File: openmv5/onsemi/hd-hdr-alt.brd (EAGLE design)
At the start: 35.6 x 16.5 mm, 54 parts, among them IC1 AR0132AT6C00XPEA0, IC2 TLV62568PDDCR, IC3 MIC5365-2.8YC5-TR, J1 DF12-36-DP, Q1 PMXB120EPEZ

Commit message: Finish out new onsemi cameras
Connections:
- removed net DCMI_D12: J1.8
- removed net DCMI_D13: J1.6
- net GND: now also J1.6, J1.8
- net SPI_MISO: now also IC1.P$35
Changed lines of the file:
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@@
 <contactref element="IC1" pad="P$55"/>
 <contactref element="IC1" pad="P$7"/>
+<contactref element="J1" pad="6"/>
+<contactref element="J1" pad="8"/>
 <wire x1="21.28" y1="11.755" x2="23.495" y2="12.9015" width="0" layer="19" extent="1-1"/>
 <wire x1="21.03" y1="10.8999" x2="21.28" y2="11.755" width="0" layer="19" extent="1-16"/>
@@
 <wire x1="20.197" y1="9.525" x2="20.28" y2="9.755" width="0" layer="19" extent="1-16"/>
 <wire x1="20.824" y1="13.208" x2="21.28" y2="11.755" width="0" layer="19" extent="1-1"/>
+<wire x1="21.03" y1="14.5001" x2="20.824" y2="13.208" width="0" layer="19" extent="1-16"/>
+<wire x1="20.53" y1="14.5001" x2="21.03" y2="14.5001" width="0" layer="19" extent="16-16"/>
+<wire x1="19.2485" y1="14.0335" x2="20.53" y2="14.5001" width="0" layer="19" extent="1-16"/>
+<wire x1="18.8" y1="13.208" x2="19.2485" y2="14.0335" width="0" layer="19" extent="1-1"/>
+<wire x1="18.288" y1="13.712" x2="18.8" y2="13.208" width="0" layer="19" extent="1-1"/>
 <wire x1="21.336" y1="8.005" x2="21.34" y2="9.525" width="0" layer="19" extent="16-16"/>
 <wire x1="20.193" y1="8.005" x2="21.336" y2="8.005" width="0" layer="19" extent="16-16"/>
@@
 <wire x1="20.7755" y1="2.54" x2="20.32" y2="4.195" width="0" layer="19" extent="1-16"/>
 <wire x1="23.0505" y1="7.6915" x2="21.336" y2="8.005" width="0" layer="19" extent="1-16"/>
-<wire x1="19.2485" y1="14.0335" x2="20.824" y2="13.208" width="0" layer="19" extent="1-1"/>
-<wire x1="18.8" y1="13.208" x2="19.2485" y2="14.0335" width="0" layer="19" extent="1-1"/>
-<wire x1="18.288" y1="13.712" x2="18.8" y2="13.208" width="0" layer="19" extent="1-1"/>
 <wire x1="15.53" y1="10.8999" x2="17.53" y2="10.8999" width="0" layer="19" extent="16-16"/>
 <wire x1="22.626" y1="1.778" x2="20.7755" y2="2.54" width="0" layer="19" extent="1-16"/>
@@
 <signal name="SPI_MISO" class="4">
 <contactref element="J1" pad="15"/>
+<contactref element="IC1" pad="P$35"/>
+<wire x1="17.28" y1="7.755" x2="18.53" y2="10.8999" width="0" layer="19" extent="1-16"/>
 </signal>
 <signal name="SPI_MOSI" class="4">
@@
 <wire x1="16.28" y1="6.755" x2="16.53" y2="14.5001" width="0" layer="19" extent="1-16"/>
 </signal>
-<signal name="DCMI_D13" class="4">
-<contactref element="J1" pad="6"/>
-</signal>
-<signal name="DCMI_D12" class="4">
-<contactref element="J1" pad="8"/>
-</signal>
 <signal name="SW" class="3">

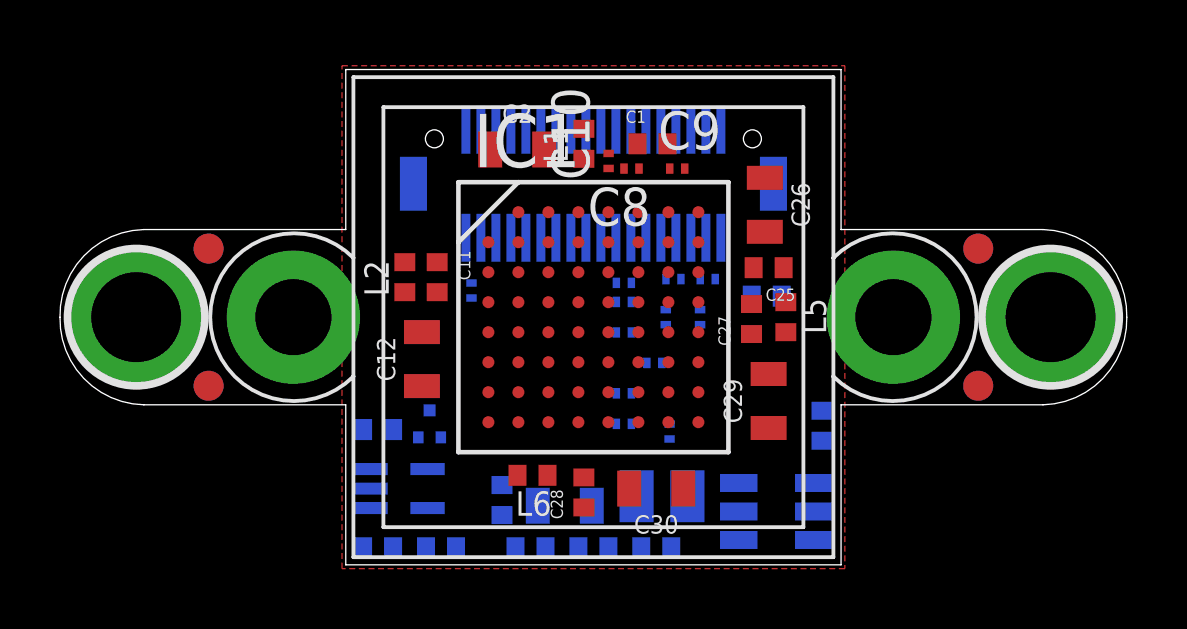
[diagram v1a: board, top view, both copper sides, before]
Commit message: Update camera modules to use different non-flippable pmosfet
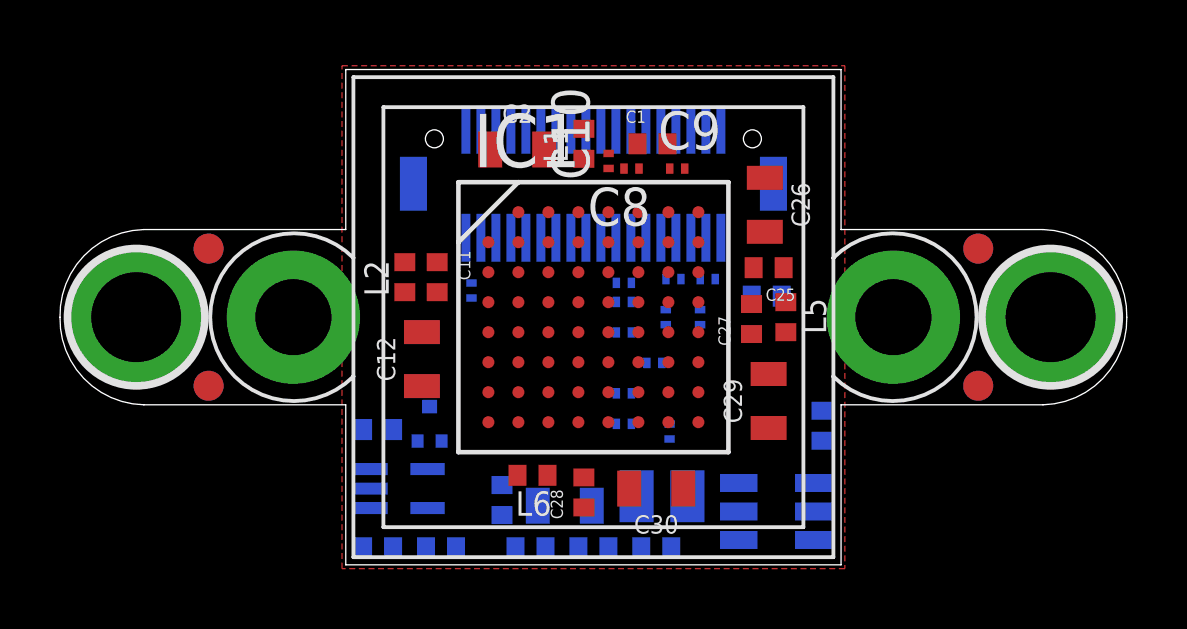
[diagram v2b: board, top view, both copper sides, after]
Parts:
- Q1: value PMXB120EPEZ -> SSM3J15FV,L3F; device PMXB120EPEZ:PMXB120EPEZ -> SSM3J15FV_L3F:SSM3J15FVL3F
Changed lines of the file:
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@@
 <attribute name="VALUE" x="15.24" y="12.954" size="0.6096" layer="27" font="vector" ratio="20" align="top-center"/>
 </element>
-<element name="Q1" library="PMXB120EPEZ" package="PMXB120EPEZ" value="PMXB120EPEZ" x="12.319" y="4.699" smashed="yes" rot="MR0">
-<attribute name="DESCRIPTION" value="MOSFET 30 V, P-channel Trench MOSFET" x="15.367" y="4.699" size="1.778" layer="28" rot="MR0" display="off"/>
-<attribute name="HEIGHT" value="0.4mm" x="15.367" y="4.699" size="1.778" layer="28" rot="MR0" display="off"/>
-<attribute name="MANUFACTURER_NAME" value="Nexperia" x="15.367" y="4.699" size="1.778" layer="28" rot="MR0" display="off"/>
-<attribute name="MANUFACTURER_PART_NUMBER" value="PMXB120EPEZ" x="15.367" y="4.699" size="1.778" layer="28" rot="MR0" display="off"/>
-<attribute name="MOUSER_PART_NUMBER" value="771-PMXB120EPEZ" x="15.367" y="4.699" size="1.778" layer="28" rot="MR0" display="off"/>
-<attribute name="MOUSER_PRICE-STOCK" value="https://www.mouser.co.uk/ProductDetail/Nexperia/PMXB120EPEZ?qs=gNSudQoqUYCYLaOobF3dPA%3D%3D" x="15.367" y="4.699" size="1.778" layer="28" rot="MR0" display="off"/>
-<attribute name="MPN" value="PMXB120EPEZ" x="15.367" y="4.699" size="1.778" layer="28" rot="MR0" display="off"/>
+<element name="Q1" library="SSM3J15FV_L3F" package="SSM3J15FVL3F" value="SSM3J15FV,L3F" x="12.319" y="4.699" smashed="yes" rot="MR0">
+<attribute name="DESCRIPTION" value="MOSFET Small-signal MOSFET High Speed Switching" x="15.367" y="4.699" size="1.778" layer="28" rot="MR0" display="off"/>
+<attribute name="HEIGHT" value="0.55mm" x="15.367" y="4.699" size="1.778" layer="28" rot="MR0" display="off"/>
+<attribute name="MANUFACTURER_NAME" value="Toshiba" x="15.367" y="4.699" size="1.778" layer="28" rot="MR0" display="off"/>
+<attribute name="MANUFACTURER_PART_NUMBER" value="SSM3J15FV,L3F" x="15.367" y="4.699" size="1.778" layer="28" rot="MR0" display="off"/>
+<attribute name="MOUSER_PART_NUMBER" value="757-SSM3J15FVL3F" x="15.367" y="4.699" size="1.778" layer="28" rot="MR0" display="off"/>
+<attribute name="MOUSER_PRICE-STOCK" value="https://www.mouser.co.uk/ProductDetail/Toshiba/SSM3J15FVL3F?qs=PDgMCp4xDJb4qTgE7FAUzA%3D%3D" x="15.367" y="4.699" size="1.778" layer="28" rot="MR0" display="off"/>
+<attribute name="MPN" value="SSM3J15FV,L3F" x="15.367" y="4.699" size="1.778" layer="28" rot="MR0" display="off"/>
 <attribute name="NAME" x="12.319" y="4.699" size="1.27" layer="26" rot="MR0" align="center"/>
 <attribute name="VALUE" x="12.319" y="4.699" size="1.27" layer="28" rot="MR0" align="center"/>
@@
 <contactref element="C24" pad="2"/>
 <contactref element="Q1" pad="2"/>
-<wire x1="10.1045" y1="0.5715" x2="10.353" y2="1.89" width="0" layer="19" extent="1-16"/>
-<wire x1="11.944" y1="4.249" x2="10.353" y2="1.89" width="0" layer="19" extent="16-16"/>
-<wire x1="21.53" y1="14.5001" x2="11.944" y2="4.249" width="0" layer="19" extent="16-16"/>
+<wire x1="11.919" y1="4.124" x2="21.53" y2="14.5001" width="0" layer="19" extent="16-16"/>
+<wire x1="10.353" y1="1.89" x2="11.919" y2="4.124" width="0" layer="19" extent="16-16"/>
+<wire x1="10.1045" y1="0.5715" x2="10.353" y2="1.89" width="0" layer="19" extent="16-16"/>
 </signal>
 <signal name="VCC" class="3">
@@
 <contactref element="J1" pad="25"/>
 <contactref element="Q1" pad="1"/>
-<wire x1="12.694" y1="4.249" x2="16.03" y2="10.8999" width="0" layer="19" extent="16-16"/>
+<wire x1="12.719" y1="4.124" x2="16.03" y2="10.8999" width="0" layer="19" extent="16-16"/>
 </signal>
 <signal name="DCMI_D4" class="4">
@@
 <contactref element="R4" pad="1"/>
 <contactref element="Q1" pad="3"/>
-<wire x1="11.1045" y1="4.5085" x2="10.353" y2="3.19" width="0" layer="19" extent="16-16"/>
-<wire x1="12.319" y1="5.149" x2="11.1045" y2="4.5085" width="0" layer="19" extent="16-16"/>
+<wire x1="11.1045" y1="4.5085" x2="12.319" y2="5.274" width="0" layer="19" extent="16-16"/>
+<wire x1="10.353" y1="3.19" x2="11.1045" y2="4.5085" width="0" layer="19" extent="16-16"/>
 </signal>
 <signal name="RESET_N" class="4">
